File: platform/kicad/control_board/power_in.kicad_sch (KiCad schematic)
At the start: 5 parts, among them J4 24V IN, J5 USB4120-03-C_REVA, U2 ACS722xLCTR-20AU

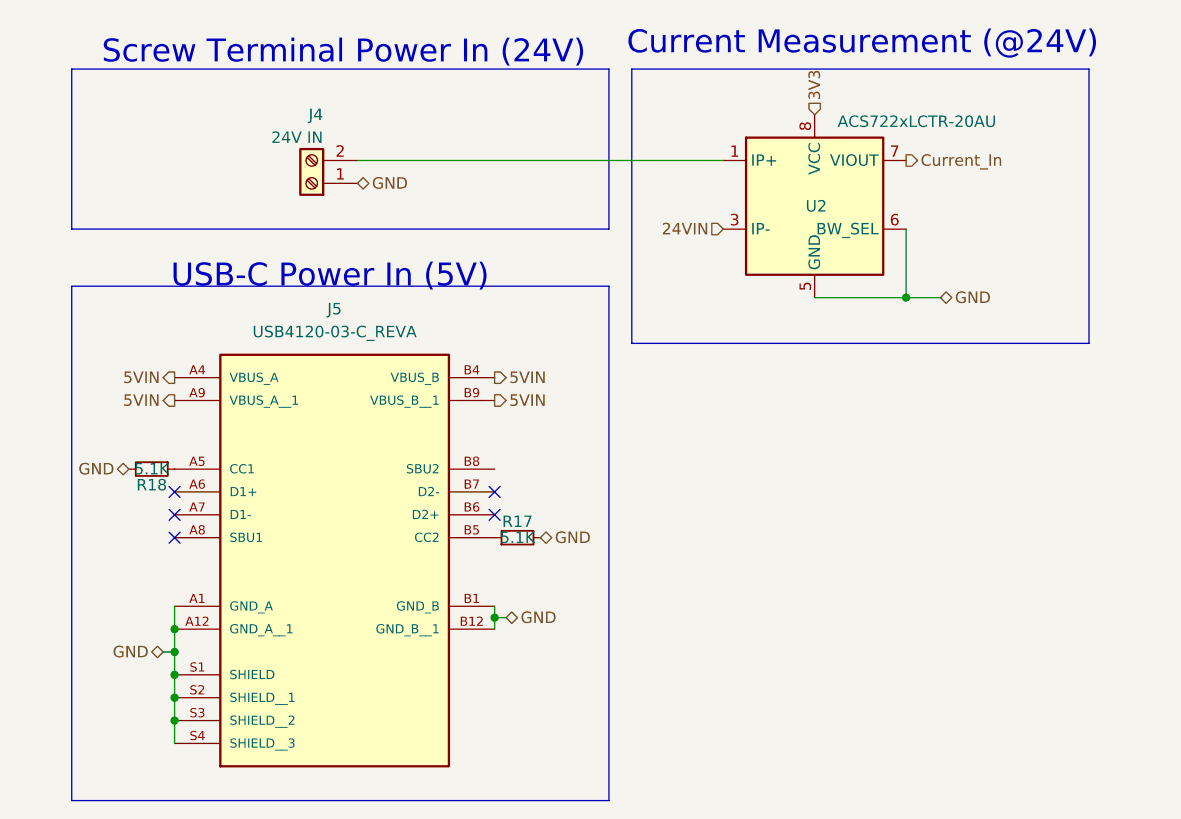
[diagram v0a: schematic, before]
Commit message: Control_PCB v4 revB: Finalised Design
This change updates the controller PCB to a finalised state, only requiring
finishing touches to be made for manufacturing.
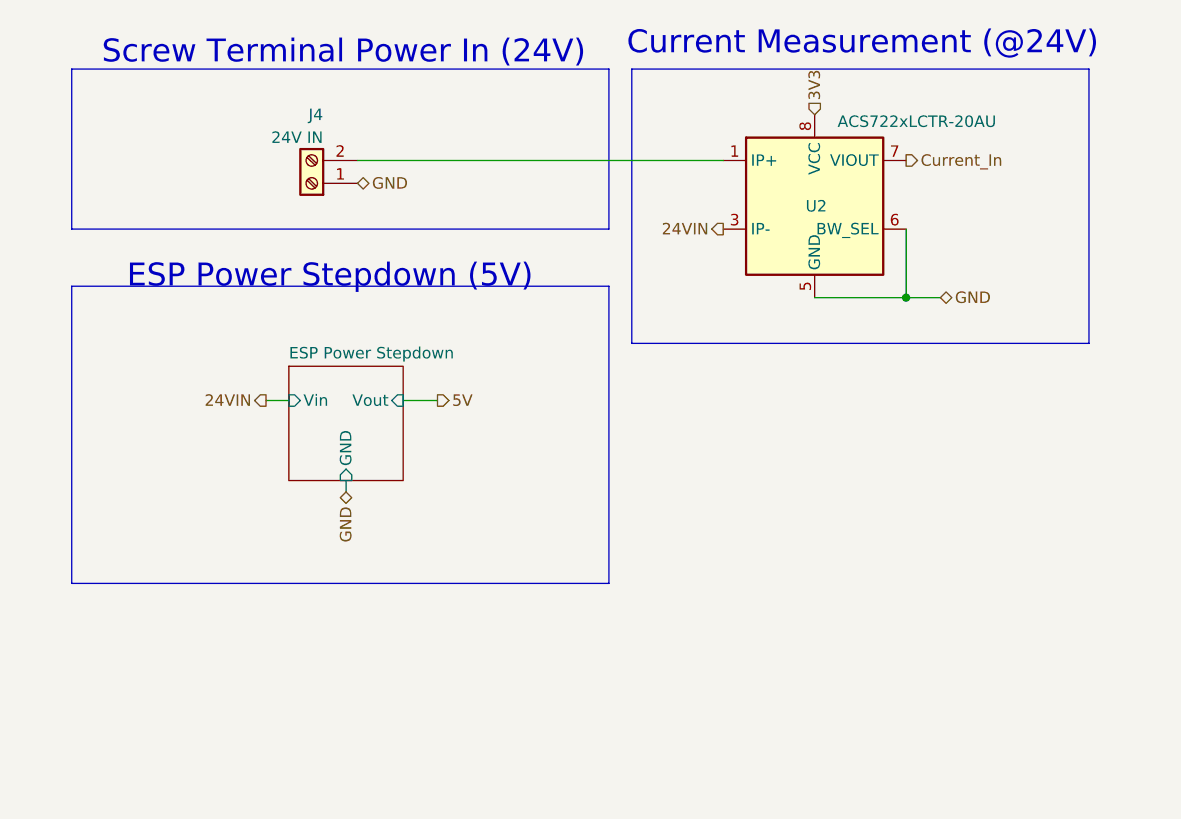
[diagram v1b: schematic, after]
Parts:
- removed J5: USB4120-03-C_REVA, AusOcean:GCT_USB4120-03-C_REVA, symbol AusOcean:USB4120-03-C_REVA
- removed R17, R18: 5.1K, Resistor_SMD:R_0201_0603Metric, symbol Device:R_Small
- J4: footprint AusOcean:CUI_Screw_terminal_1x2 -> AusOcean:CUI_TB005-762-02BE
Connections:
- no-connect marks 5 -> 0
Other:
- added sheet ESP Power Stepdown (stepdown.kicad_sch)
- note added: "ESP Power Stepdown (5V)"
- note removed: "USB-C Power In (5V)"
